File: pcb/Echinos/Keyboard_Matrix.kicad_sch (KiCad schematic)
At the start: 62 parts, among them J5 Joystick

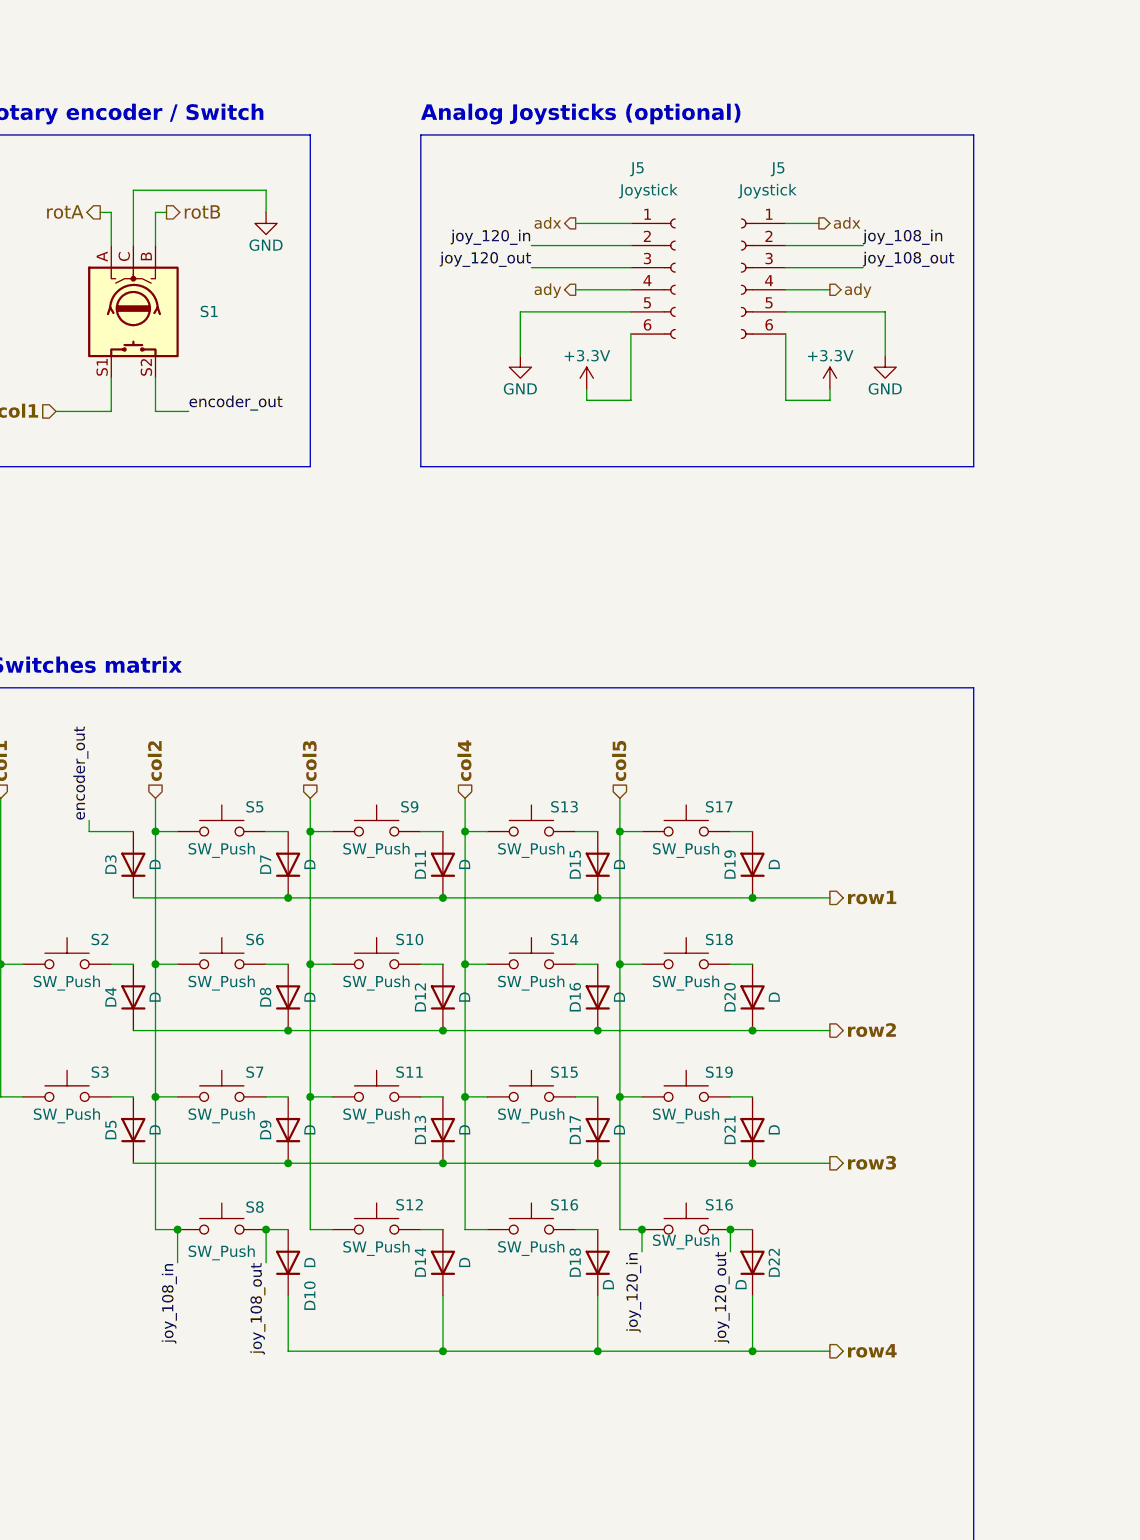
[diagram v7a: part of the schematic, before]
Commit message: 🚧 [PCB] - Backup before trying to add 5.0V support.
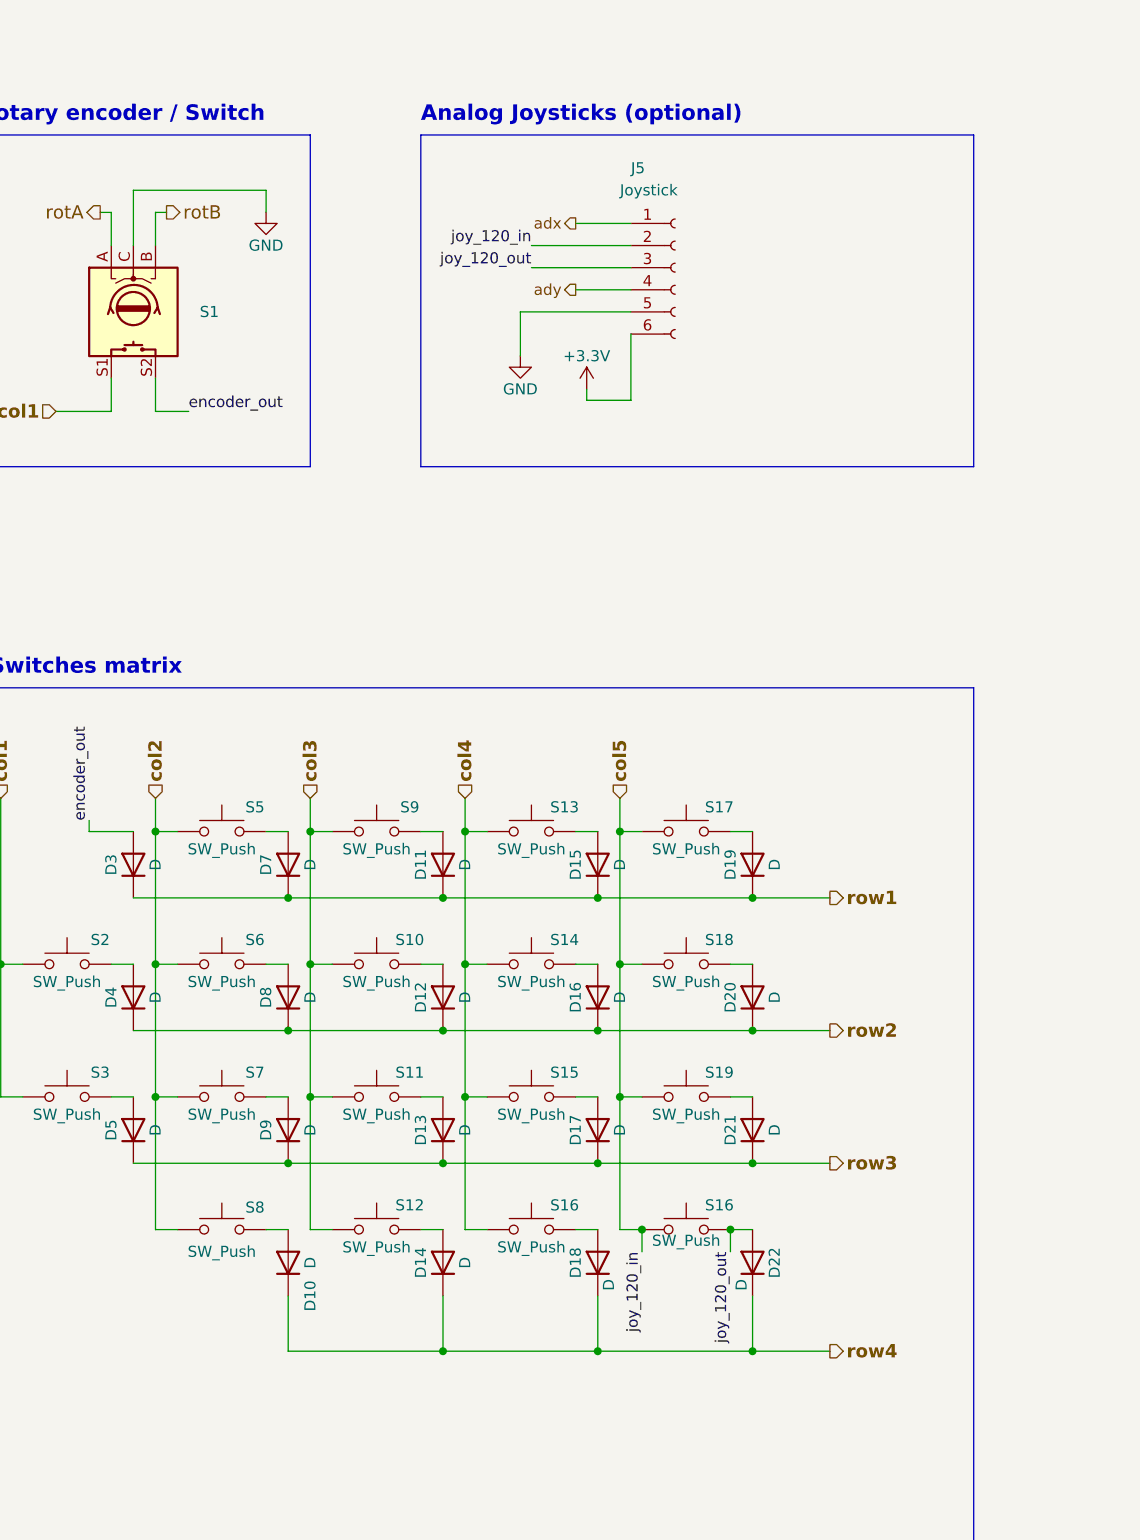
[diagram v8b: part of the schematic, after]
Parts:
- removed J5: Joystick, Echinos:Joystick_KSilver_JP19, symbol Connector:Conn_01x06_Socket
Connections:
- net joy_108_out: no longer names the net of D10.2 (A), S8.2
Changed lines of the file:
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@@
   (junction (at 96.52 143.51) (diameter 0) (color 0 0 0 0)
   )
-  (junction (at 58.42 151.13) (diameter 0) (color 0 0 0 0)
-  )
   (junction (at 114.3 113.03) (diameter 0) (color 0 0 0 0)
   )
@@
   )
   (junction (at 78.74 143.51) (diameter 0) (color 0 0 0 0)
-  )
-  (junction (at 48.26 151.13) (diameter 0) (color 0 0 0 0)
   )
   (junction (at 60.96 113.03) (diameter 0) (color 0 0 0 0)
@@
     (stroke (width 0) (type default))
   )
-  (wire (pts (xy 118.11 38.1) (xy 127 38.1))
-    (stroke (width 0) (type default))
-  )
   (wire (pts (xy 204.47 -39.37) (xy 224.79 -39.37))
     (stroke (width 0) (type default))
@@
     (stroke (width 0) (type default))
   )
-  (wire (pts (xy 129.54 50.8) (xy 129.54 45.72))
-    (stroke (width 0) (type default))
-  )
   (wire (pts (xy 45.72 135.89) (xy 45.72 151.13))
     (stroke (width 0) (type default))
@@
     (stroke (width 0) (type default))
   )
-  (wire (pts (xy 118.11 43.18) (xy 123.19 43.18))
-    (stroke (width 0) (type default))
-  )
   (wire (pts (xy 93.98 151.13) (xy 96.52 151.13))
     (stroke (width 0) (type default))
@@
     (stroke (width 0) (type default))
   )
-  (wire (pts (xy 129.54 45.72) (xy 118.11 45.72))
-    (stroke (width 0) (type default))
-  )
   (wire (pts (xy 101.6 151.13) (xy 101.6 153.67))
     (stroke (width 0) (type default))
@@
     (stroke (width 0) (type default))
   )
-  (wire (pts (xy 123.19 55.88) (xy 123.19 54.61))
-    (stroke (width 0) (type default))
-  )
   (wire (pts (xy 43.18 143.51) (xy 60.96 143.51))
     (stroke (width 0) (type default))
@@
     (stroke (width 0) (type default))
   )
-  (wire (pts (xy 118.11 40.64) (xy 127 40.64))
-    (stroke (width 0) (type default))
-  )
   (wire (pts (xy 54.61 -54.61) (xy 62.23 -54.61))
     (stroke (width 0) (type default))
@@
     (stroke (width 0) (type default))
   )
-  (wire (pts (xy 118.11 48.26) (xy 118.11 55.88))
-    (stroke (width 0) (type default))
-  )
   (wire (pts (xy 69.85 -46.99) (xy 74.93 -46.99))
     (stroke (width 0) (type default))
@@
     (stroke (width 0) (type default))
   )
-  (wire (pts (xy 58.42 154.94) (xy 58.42 151.13))
-    (stroke (width 0) (type default))
-  )
   (wire (pts (xy 87.63 45.72) (xy 87.63 50.8))
     (stroke (width 0) (type default))
@@
     (stroke (width 0) (type default))
   )
-  (wire (pts (xy 48.26 154.94) (xy 48.26 151.13))
-    (stroke (width 0) (type default))
-  )
   (wire (pts (xy 63.5 135.89) (xy 63.5 151.13))
     (stroke (width 0) (type default))
@@
     (stroke (width 0) (type default))
   )
-  (wire (pts (xy 118.11 55.88) (xy 123.19 55.88))
-    (stroke (width 0) (type default))
-  )
   (wire (pts (xy 184.15 -39.37) (xy 204.47 -39.37))
     (stroke (width 0) (type default))
@@
   )
   (wire (pts (xy 40.64 34.29) (xy 39.37 34.29))
-    (stroke (width 0) (type default))
-  )
-  (wire (pts (xy 118.11 35.56) (xy 121.92 35.56))
     (stroke (width 0) (type default))
   )
@@
     (effects (font (size 1.27 1.27)) (justify right bottom))
   )
-  (label "joy_108_in" (at 127 38.1 0) (fields_autoplaced)
-    (effects (font (size 1.27 1.27)) (justify left bottom))
-  )
   (label "encoder_out" (at 49.53 57.15 0) (fields_autoplaced)
     (effects (font (size 1.27 1.27)) (justify left bottom))
   )
-  (label "joy_108_out" (at 127 40.64 0) (fields_autoplaced)
-    (effects (font (size 1.27 1.27)) (justify left bottom))
-  )
-  (label "joy_108_in" (at 48.26 154.94 270) (fields_autoplaced)
-    (effects (font (size 1.27 1.27)) (justify right bottom))
-  )
   (label "joy_120_out" (at 111.76 153.67 270) (fields_autoplaced)
     (effects (font (size 1.27 1.27)) (justify right bottom))
   )
-  (label "joy_108_out" (at 58.42 154.94 270) (fields_autoplaced)
-    (effects (font (size 1.27 1.27)) (justify right bottom))
-  )
   (label "joy_120_in" (at 88.9 38.1 180) (fields_autoplaced)
     (effects (font (size 1.27 1.27)) (justify right bottom))
@@
   (hierarchical_label "col3" (shape input) (at 63.5 101.6 90) (fields_autoplaced)
     (effects (font (size 1.524 1.524) (thickness 0.3048) bold) (justify left))
-  )
-  (hierarchical_label "adx" (shape output) (at 121.92 35.56 0) (fields_autoplaced)
-    (effects (font (size 1.27 1.27)) (justify left))
-  )
-  (hierarchical_label "ady" (shape output) (at 123.19 43.18 0) (fields_autoplaced)
-    (effects (font (size 1.27 1.27)) (justify left))
   )
   (hierarchical_label "row2" (shape output) (at 123.19 128.27 0) (fields_autoplaced)
@@
     )
   )
-  (symbol (lib_id "power:GND") (at 129.54 50.8 0) (unit 1)
-    (in_bom yes) (on_board yes) (dnp no)
-    (property "Reference" "#PWR038" (at 129.54 57.15 0)
-      (effects (font (size 1.27 1.27)) hide)
-    )
-    (property "Value" "GND" (at 129.54 54.61 0)
-      (effects (font (size 1.27 1.27)))
-    )
-    (property "Footprint" "" (at 129.54 50.8 0)
-      (effects (font (size 1.27 1.27)) hide)
-    )
-    (property "Datasheet" "" (at 129.54 50.8 0)
-      (effects (font (size 1.27 1.27)) hide)
-    )
-    (pin "1")
-    (instances
-      (project "Echinos"
-        (path "/5bd3006d-ec09-4ffb-bec3-03fa5613b46a/82089e05-aeac-4bc0-b466-29ce28ef1ab1"
-          (reference "#PWR038") (unit 1)
-        )
-        (path "/5bd3006d-ec09-4ffb-bec3-03fa5613b46a/82089e05-aeac-4bc0-b466-29ce28ef1ab1/68cfefc1-3239-4b03-a7c8-c56ddb495d3c"
-          (reference "#PWR028") (unit 1)
-        )
-      )
-      (project "ptechinos"
-        (path "/e63e39d7-6ac0-4ffd-8aa3-1841a4541b55"
-          (reference "#PWR012") (unit 1)
-        )
-      )
-    )
-  )
   (symbol (lib_id "Device:D") (at 43.18 139.7 90) (unit 1)
     (in_bom yes) (on_board yes) (dnp no)
@@
     )
   )
-  (symbol (lib_id "power:+3.3V") (at 123.19 54.61 0) (unit 1)
-    (in_bom yes) (on_board yes) (dnp no)
-    (property "Reference" "#PWR034" (at 123.19 58.42 0)
-      (effects (font (size 1.27 1.27)) hide)
-    )
-    (property "Value" "+3.3V" (at 123.19 50.8 0)
-      (effects (font (size 1.27 1.27)))
-    )
-    (property "Footprint" "" (at 123.19 54.61 0)
-      (effects (font (size 1.27 1.27)) hide)
-    )
-    (property "Datasheet" "" (at 123.19 54.61 0)
-      (effects (font (size 1.27 1.27)) hide)
-    )
-    (pin "1")
-    (instances
-      (project "Echinos"
-        (path "/5bd3006d-ec09-4ffb-bec3-03fa5613b46a"
-          (reference "#PWR034") (unit 1)
-        )
-        (path "/5bd3006d-ec09-4ffb-bec3-03fa5613b46a/82089e05-aeac-4bc0-b466-29ce28ef1ab1"
-          (reference "#PWR039") (unit 1)
-        )
-        (path "/5bd3006d-ec09-4ffb-bec3-03fa5613b46a/82089e05-aeac-4bc0-b466-29ce28ef1ab1/68cfefc1-3239-4b03-a7c8-c56ddb495d3c"
-          (reference "#PWR012") (unit 1)
-        )
-      )
-    )
-  )
   (symbol (lib_id "LED:SK6812MINI") (at 224.79 -46.99 0) (unit 1)
     (in_bom yes) (on_board yes) (dnp no)
@@
         )
       )
-    )
-  )
-  (symbol (lib_id "Connector:Conn_01x06_Socket") (at 113.03 40.64 0) (mirror y) (unit 1)
-    (in_bom yes) (on_board yes) (dnp no)
-    (property "Reference" "J5" (at 118.11 29.21 0)
-      (effects (font (size 1.27 1.27)) (justify left))
-    )
-    (property "Value" "Joystick" (at 119.38 31.75 0)
-      (effects (font (size 1.27 1.27)) (justify left))
-    )
-    (property "Footprint" "Echinos:Joystick_KSilver_JP19" (at 113.03 40.64 0)
-      (effects (font (size 1.27 1.27)) hide)
-    )
-    (property "Datasheet" "~" (at 113.03 40.64 0)
-      (effects (font (size 1.27 1.27)) hide)
-    )
-    (pin "1")
-    (pin "2")
-    (pin "3")
-    (pin "4")
-    (pin "5")
-    (pin "6")
-    (instances
-      (project "Echinos"
-        (path "/5bd3006d-ec09-4ffb-bec3-03fa5613b46a/82089e05-aeac-4bc0-b466-29ce28ef1ab1"
-          (reference "J5") (unit 1)
-        )
-        (path "/5bd3006d-ec09-4ffb-bec3-03fa5613b46a/82089e05-aeac-4bc0-b466-29ce28ef1ab1/68cfefc1-3239-4b03-a7c8-c56ddb495d3c"
-          (reference "JW108") (unit 1)
-        )
-      )
